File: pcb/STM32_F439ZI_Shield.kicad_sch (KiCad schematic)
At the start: 19 parts, among them K1 G6S-2, K2 G6S-2, U1 LM2904, U13 R-78E3.3-0.5, U14 R-78E5.0-0.5, U2 MAX3485

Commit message: updated pcb
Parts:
- removed U14: R-78E5.0-0.5, Converter_DCDC:Converter_DCDC_RECOM_R-78E-0.5_THT, symbol Regulator_Switching:R-78E5.0-0.5
- added C10: 22n, Capacitor_SMD:C_1206_3216Metric, symbol Device:C_Small
- added J3: Relais_Conn, TerminalBlock_TE-Connectivity:TerminalBlock_TE_282834-2_1x02_P2.54mm_Horizontal, symbol Connector:Conn_01x02_Pin
- added J4, J5: Conn_01x02_Pin, TerminalBlock_TE-Connectivity:TerminalBlock_TE_282834-2_1x02_P2.54mm_Horizontal, symbol Connector:Conn_01x02_Pin
- added R43: 150, Resistor_SMD:R_1206_3216Metric, symbol Device:R
- Spannungsversorgung_1: footprint Connector_Phoenix_MSTB:PhoenixContact_MSTBA_2,5_2-G-5,08_1x02_P5.08mm_Horizontal -> TerminalBlock_TE-Connectivity:TerminalBlock_TE_282834-2_1x02_P2.54mm_Horizontal
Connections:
- net GND: now also C10.2, J4.1 (Pin_1), J5.2 (Pin_2), R43.2
- net Optokoppler/IN0_MCU_IN: now also K2.3; no longer K2.4
- net Optokoppler/IN1_MCU_IN: now also K1.3; no longer K1.4
- net STM32F439ZI/IN0_MCU: now also K2.4; no longer K2.3
- net STM32F439ZI/IN1_MCU: now also K1.4; no longer K1.3
- net STM32F439ZI/Endschalter_Vorne_MCU: now reaches K2.5
- net STM32F439ZI/Endschalter_Hinten_MCU: now reaches K1.5
- net Endschalter/Endschalter_Hinten_IN_1 renamed Endschalter/Endschalter_Hinten
- net Endschalter/Endschalter_Vorne_IN_1 renamed Endschalter/Endschalter_Vorne
- new net Optokoppler/Ext_Relais1_OUT: J3.1 (Pin_1)
- new net Optokoppler/Ext_Relais2_OUT: J3.2 (Pin_2)
- new net STM32F439ZI/Opt_Analog_IN: J5.1 (Pin_1)
- new net STM32F439ZI/Opt_Temperaturmessung: C10.1, J4.2 (Pin_2), R43.1
- no-connect marks 0 -> 6
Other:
- sheet Buttons renamed Buttons_LEDS
- sheet Buttons_LEDS ports: added MCU_Kalibrierung, MCU_LED_Betrieb, MCU_LED_Kalibrierung, MCU_LED_Manuell, MCU_LED_PWR, MCU_LED_Rollen, MCU_LED_Stoerung, MCU_LED_Trimmen, MCU_Switch, MCU_Vorfahren, MCU_Zurueckfahren; removed MCU_Button1, MCU_Button2, MCU_Button3, MCU_Button4, MCU_LED_Gelb, MCU_LED_Green1, MCU_LED_Green2, MCU_LED_Red
- sheet Endschalter ports: added Endschalter_Hinten, Endschalter_Vorne; removed Endschalter_Hinten_IN_1, Endschalter_Vorne_IN_1
- sheet Optokoppler ports: added Ext_Relais1_MCU, Ext_Relais1_OUT, Ext_Relais2_MCU, Ext_Relais2_OUT; removed Endschalter_Hinten_HV_IN, Endschalter_Hinten_MCU, Endschalter_Vorne_HV_IN, Endschalter_Vorne_MCU
- sheet STM32F439ZI ports: added LED_5, LED_6, LED_7, Opt_Analog_IN, Opt_Temperaturmessung, ext_Relais_1, ext_Relais_2; removed none
- moved on the sheet: C1, C2, C3, C4, C5, C6, F1, K1, K2, R10, R6, R7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

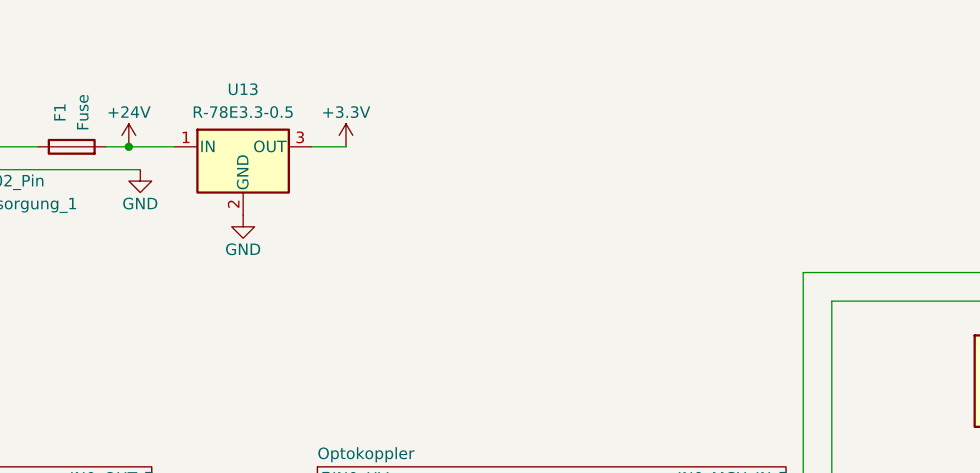
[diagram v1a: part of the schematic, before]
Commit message: added voltage regulator updated pinout
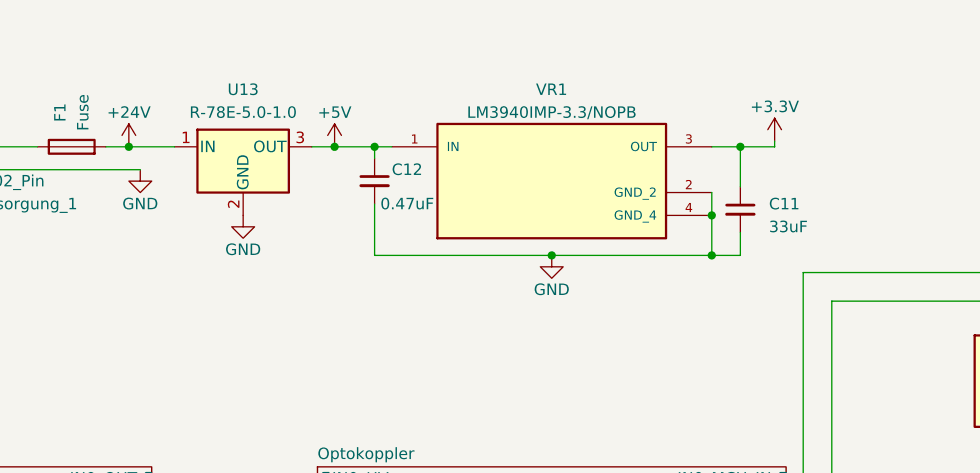
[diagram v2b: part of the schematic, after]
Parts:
- added C11: 33uF, Capacitor_SMD:C_1206_3216Metric, symbol Device:C_Small
- added C12: 0.47uF, Capacitor_SMD:C_1206_3216Metric, symbol Device:C_Small
- added VR1: LM3940IMP-3.3/NOPB, LM3940IMP-3.3_NOPB:VREG_LM3940IMP-3.3_NOPB, symbol LM3940IMP-3.3_NOPB:LM3940IMP-3.3/NOPB
- U13: value R-78E3.3-0.5 -> R-78E-5.0-1.0
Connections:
- net +3.3V: now also C11.1, VR1.3 (OUT); no longer U13.3 (OUT)
- net GND: now also C11.2, C12.2, VR1.2 (GND_2), VR1.4 (GND_4)
- new net +5V: C12.1, U13.3 (OUT), VR1.1 (IN)

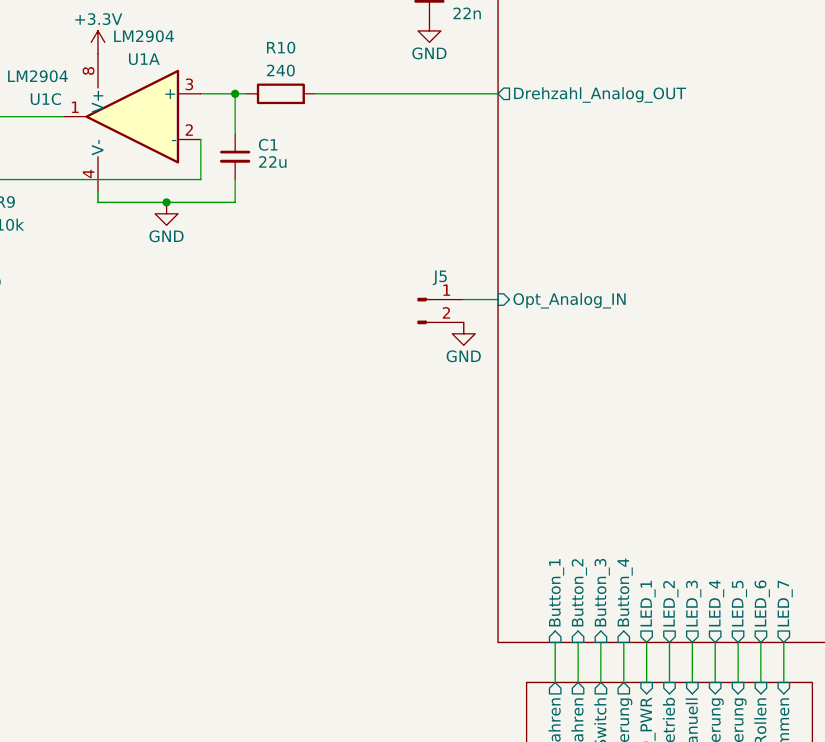
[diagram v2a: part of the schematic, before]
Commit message: updated pcb and assigned correct pins
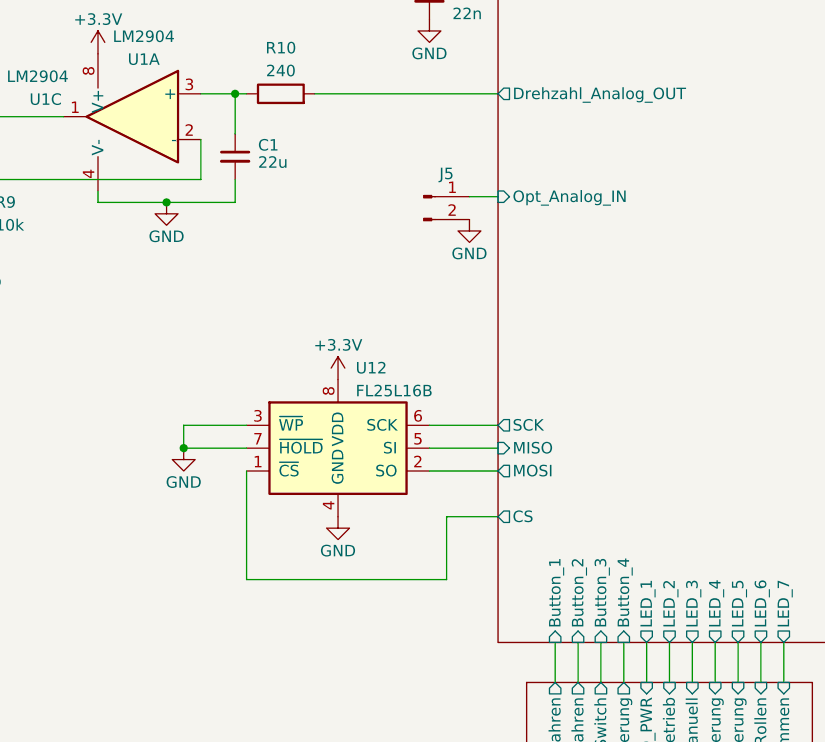
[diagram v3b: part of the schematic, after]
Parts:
- added U12: FL25L16B, SOIC127P602X172-8N:SOIC127P602X172-8N, symbol Memory_NVRAM:MB85RS16
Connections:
- net +3.3V: now also U12.8 (VDD)
- net GND: now also U12.3 (~{WP}), U12.4 (GND), U12.7 (~{HOLD})
- new net STM32F439ZI/CS: U12.1 (~{CS})
- new net STM32F439ZI/MISO: U12.5 (SI)
- new net STM32F439ZI/MOSI: U12.2 (SO)
- new net STM32F439ZI/SCK: U12.6 (SCK)
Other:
- sheet STM32F439ZI ports: added CS, MISO, MOSI, SCK; removed none
- moved on the sheet: J5
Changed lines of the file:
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@@
   (junction (at 104.775 104.14) (diameter 0) (color 0 0 0 0)
+  )
+  (junction (at 99.06 143.51) (diameter 0) (color 0 0 0 0)
   )
   (junction (at 126.365 90.17) (diameter 0) (color 0 0 0 0)
@@
     (stroke (width 0) (type default))
   )
+  (wire (pts (xy 128.27 158.115) (xy 128.27 151.13))
+    (stroke (width 0) (type default))
+  )
   (wire (pts (xy 243.205 122.555) (xy 252.095 122.555))
     (stroke (width 0) (type default))
@@
     (stroke (width 0) (type default))
   )
+  (wire (pts (xy 126.365 140.97) (xy 133.985 140.97))
+    (stroke (width 0) (type default))
+  )
   (wire (pts (xy 105.41 29.21) (xy 105.41 31.75))
     (stroke (width 0) (type default))
@@
     (stroke (width 0) (type default))
   )
+  (wire (pts (xy 106.045 143.51) (xy 99.06 143.51))
+    (stroke (width 0) (type default))
+  )
   (wire (pts (xy 236.855 77.47) (xy 236.855 80.01))
     (stroke (width 0) (type default))
@@
     (stroke (width 0) (type default))
   )
+  (wire (pts (xy 106.045 158.115) (xy 128.27 158.115))
+    (stroke (width 0) (type default))
+  )
   (wire (pts (xy 204.47 144.145) (xy 204.47 145.415))
     (stroke (width 0) (type default))
@@
     (stroke (width 0) (type default))
   )
+  (wire (pts (xy 99.06 140.97) (xy 106.045 140.97))
+    (stroke (width 0) (type default))
+  )
   (wire (pts (xy 215.265 41.275) (xy 215.265 76.835))
     (stroke (width 0) (type default))
@@
     (stroke (width 0) (type default))
   )
+  (wire (pts (xy 99.06 143.51) (xy 99.06 140.97))
+    (stroke (width 0) (type default))
+  )
   (wire (pts (xy 177.8 33.655) (xy 177.8 42.545))
     (stroke (width 0) (type default))
@@
     (stroke (width 0) (type default))
   )
+  (wire (pts (xy 126.365 146.05) (xy 133.985 146.05))
+    (stroke (width 0) (type default))
+  )
+  (wire (pts (xy 128.27 151.13) (xy 133.985 151.13))
+    (stroke (width 0) (type default))
+  )
   (wire (pts (xy 158.115 165.1) (xy 158.115 169.545))
     (stroke (width 0) (type default))
@@
     (stroke (width 0) (type default))
   )
+  (wire (pts (xy 126.365 143.51) (xy 133.985 143.51))
+    (stroke (width 0) (type default))
+  )
   (wire (pts (xy 185.42 42.545) (xy 185.42 38.1))
     (stroke (width 0) (type default))
@@
     (stroke (width 0) (type default))
   )
-  (wire (pts (xy 130.175 127) (xy 133.985 127))
+  (wire (pts (xy 130.81 115.57) (xy 133.985 115.57))
     (stroke (width 0) (type default))
   )
@@
   )
   (wire (pts (xy 190.5 42.545) (xy 190.5 41.275))
+    (stroke (width 0) (type default))
+  )
+  (wire (pts (xy 106.045 146.05) (xy 106.045 158.115))
     (stroke (width 0) (type default))
   )
@@
     )
   )
-  (symbol (lib_id "Connector:Conn_01x02_Pin") (at 125.095 127 0) (unit 1)
-    (in_bom yes) (on_board yes) (dnp no)
-    (property "Reference" "J5" (at 127.635 124.46 0)
-      (effects (font (size 1.27 1.27)))
-    )
-    (property "Value" "Conn_01x02_Pin" (at 127.635 132.08 0)
-      (effects (font (size 1.27 1.27)) hide)
-    )
-    (property "Footprint" "TerminalBlock_TE-Connectivity:TerminalBlock_TE_282834-2_1x02_P2.54mm_Horizontal" (at 125.095 127 0)
-      (effects (font (size 1.27 1.27)) hide)
-    )
-    (property "Datasheet" "~" (at 125.095 127 0)
+  (symbol (lib_id "Connector:Conn_01x02_Pin") (at 125.73 115.57 0) (unit 1)
+    (in_bom yes) (on_board yes) (dnp no)
+    (property "Reference" "J5" (at 128.27 113.03 0)
+      (effects (font (size 1.27 1.27)))
+    )
+    (property "Value" "Conn_01x02_Pin" (at 128.27 120.65 0)
+      (effects (font (size 1.27 1.27)) hide)
+    )
+    (property "Footprint" "TerminalBlock_TE-Connectivity:TerminalBlock_TE_282834-2_1x02_P2.54mm_Horizontal" (at 125.73 115.57 0)
+      (effects (font (size 1.27 1.27)) hide)
+    )
+    (property "Datasheet" "~" (at 125.73 115.57 0)
       (effects (font (size 1.27 1.27)) hide)
     )
@@
         (path "/19bff231-ff37-4a40-bd06-2039e9f55c77"
           (reference "C5") (unit 1)
+        )
+      )
+    )
+  )
+  (symbol (lib_id "power:GND") (at 99.06 143.51 0) (unit 1)
+    (in_bom yes) (on_board yes) (dnp no)
+    (property "Reference" "#PWR095" (at 99.06 149.86 0)
+      (effects (font (size 1.27 1.27)) hide)
+    )
+    (property "Value" "GND" (at 99.06 147.32 0)
+      (effects (font (size 1.27 1.27)))
+    )
+    (property "Footprint" "" (at 99.06 143.51 0)
+      (effects (font (size 1.27 1.27)) hide)
+    )
+    (property "Datasheet" "" (at 99.06 143.51 0)
+      (effects (font (size 1.27 1.27)) hide)
+    )
+    (pin "1")
+    (instances
+      (project "STM32_F439ZI_Shield"
+        (path "/19bff231-ff37-4a40-bd06-2039e9f55c77"
+          (reference "#PWR095") (unit 1)
+        )
+      )
+    )
+  )
+  (symbol (lib_id "power:GND") (at 116.205 151.13 0) (unit 1)
+    (in_bom yes) (on_board yes) (dnp no)
+    (property "Reference" "#PWR094" (at 116.205 157.48 0)
+      (effects (font (size 1.27 1.27)) hide)
+    )
+    (property "Value" "GND" (at 116.205 154.94 0)
+      (effects (font (size 1.27 1.27)))
+    )
+    (property "Footprint" "" (at 116.205 151.13 0)
+      (effects (font (size 1.27 1.27)) hide)
+    )
+    (property "Datasheet" "" (at 116.205 151.13 0)
+      (effects (font (size 1.27 1.27)) hide)
+    )
+    (pin "1")
+    (instances
+      (project "STM32_F439ZI_Shield"
+        (path "/19bff231-ff37-4a40-bd06-2039e9f55c77"
+          (reference "#PWR094") (unit 1)
         )
       )
@@
     )
   )
-  (symbol (lib_id "power:GND") (at 130.175 129.54 0) (unit 1)
-    (in_bom yes) (on_board yes) (dnp no)
-    (property "Reference" "#PWR034" (at 130.175 135.89 0)
-      (effects (font (size 1.27 1.27)) hide)
-    )
-    (property "Value" "GND" (at 130.175 133.35 0)
-      (effects (font (size 1.27 1.27)))
-    )
-    (property "Footprint" "" (at 130.175 129.54 0)
-      (effects (font (size 1.27 1.27)) hide)
-    )
-    (property "Datasheet" "" (at 130.175 129.54 0)
+  (symbol (lib_id "power:GND") (at 130.81 118.11 0) (unit 1)
+    (in_bom yes) (on_board yes) (dnp no)
+    (property "Reference" "#PWR034" (at 130.81 124.46 0)
+      (effects (font (size 1.27 1.27)) hide)
+    )
+    (property "Value" "GND" (at 130.81 121.92 0)
+      (effects (font (size 1.27 1.27)))
+    )
+    (property "Footprint" "" (at 130.81 118.11 0)
+      (effects (font (size 1.27 1.27)) hide)
+    )
+    (property "Datasheet" "" (at 130.81 118.11 0)
       (effects (font (size 1.27 1.27)) hide)
     )
@@
     )
   )
+  (symbol (lib_id "power:+3.3V") (at 116.205 135.89 0) (unit 1)
+    (in_bom yes) (on_board yes) (dnp no) (fields_autoplaced)
+    (property "Reference" "#PWR093" (at 116.205 139.7 0)
+      (effects (font (size 1.27 1.27)) hide)
+    )
+    (property "Value" "+3.3V" (at 116.205 132.08 0)
+      (effects (font (size 1.27 1.27)))
+    )
+    (property "Footprint" "" (at 116.205 135.89 0)
+      (effects (font (size 1.27 1.27)) hide)
+    )
+    (property "Datasheet" "" (at 116.205 135.89 0)
+      (effects (font (size 1.27 1.27)) hide)
+    )
+    (pin "1")
+    (instances
+      (project "STM32_F439ZI_Shield"
+        (path "/19bff231-ff37-4a40-bd06-2039e9f55c77"
+          (reference "#PWR093") (unit 1)
+        )
+      )
+    )
+  )
   (symbol (lib_id "Connector:Conn_01x02_Pin") (at 225.425 140.335 180) (unit 1)
     (in_bom yes) (on_board yes) (dnp no)
@@
         (path "/19bff231-ff37-4a40-bd06-2039e9f55c77/627cdbea-55a6-4b71-bf1e-ff5bf9a61719"
           (reference "R4") (unit 1)
+        )
+      )
+    )
+  )
+  (symbol (lib_id "Memory_NVRAM:MB85RS16") (at 116.205 143.51 0) (unit 1)
+    (in_bom yes) (on_board yes) (dnp no)
+    (property "Reference" "U12" (at 118.1609 134.62 0)
+      (effects (font (size 1.27 1.27)) (justify left))
+    )
+    (property "Value" "FL25L16B" (at 118.1609 137.16 0)
+      (effects (font (size 1.27 1.27)) (justify left))
+    )
+    (property "Footprint" "SOIC127P602X172-8N:SOIC127P602X172-8N" (at 107.315 144.78 0)
+      (effects (font (size 1.27 1.27)) hide)
+    )
+    (property "Datasheet" "http://www.fujitsu.com/downloads/MICRO/fsa/pdf/products/memory/fram/MB85RS16-DS501-00014-6v0-E.pdf" (at 107.315 144.78 0)
+      (effects (font (size 1.27 1.27)) hide)
+    )
+    (pin "1")
+    (pin "2")
+    (pin "3")
+    (pin "4")
+    (pin "5")
+    (pin "6")
+    (pin "7")
+    (pin "8")
+    (instances
+      (project "STM32_F439ZI_Shield"
+        (path "/19bff231-ff37-4a40-bd06-2039e9f55c77"
+          (reference "U12") (unit 1)
         )
       )
@@
       (effects (font (size 1.27 1.27)) (justify left))
     )
-    (pin "Opt_Analog_IN" input (at 133.985 127 180)
-      (effects (font (size 1.27 1.27)) (justify left))
-    )
+    (pin "Opt_Analog_IN" input (at 133.985 115.57 180)
+      (effects (font (size 1.27 1.27)) (justify left))
+    )
+    (pin "CS" output (at 133.985 151.13 180)
+      (effects (font (size 1.27 1.27)) (justify left))
+    )
+    (pin "SCK" output (at 133.985 140.97 180)
+      (effects (font (size 1.27 1.27)) (justify left))
+    )
+    (pin "MISO" input (at 133.985 143.51 180)
+      (effects (font (size 1.27 1.27)) (justify left))
+    )
+    (pin "MOSI" output (at 133.985 146.05 180)
+      (effects (font (size 1.27 1.27)) (justify left))
+    )
